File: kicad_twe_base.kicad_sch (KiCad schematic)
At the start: 9 parts, among them J1 Conn_01x14, J2 Conn_01x14, J3 Conn_01x07, SW1 SW_SPDT, SW2 SW_Push, SW3 SW_SPDT, U1 BHC-CR123A, U2 TWE-L-DP-W

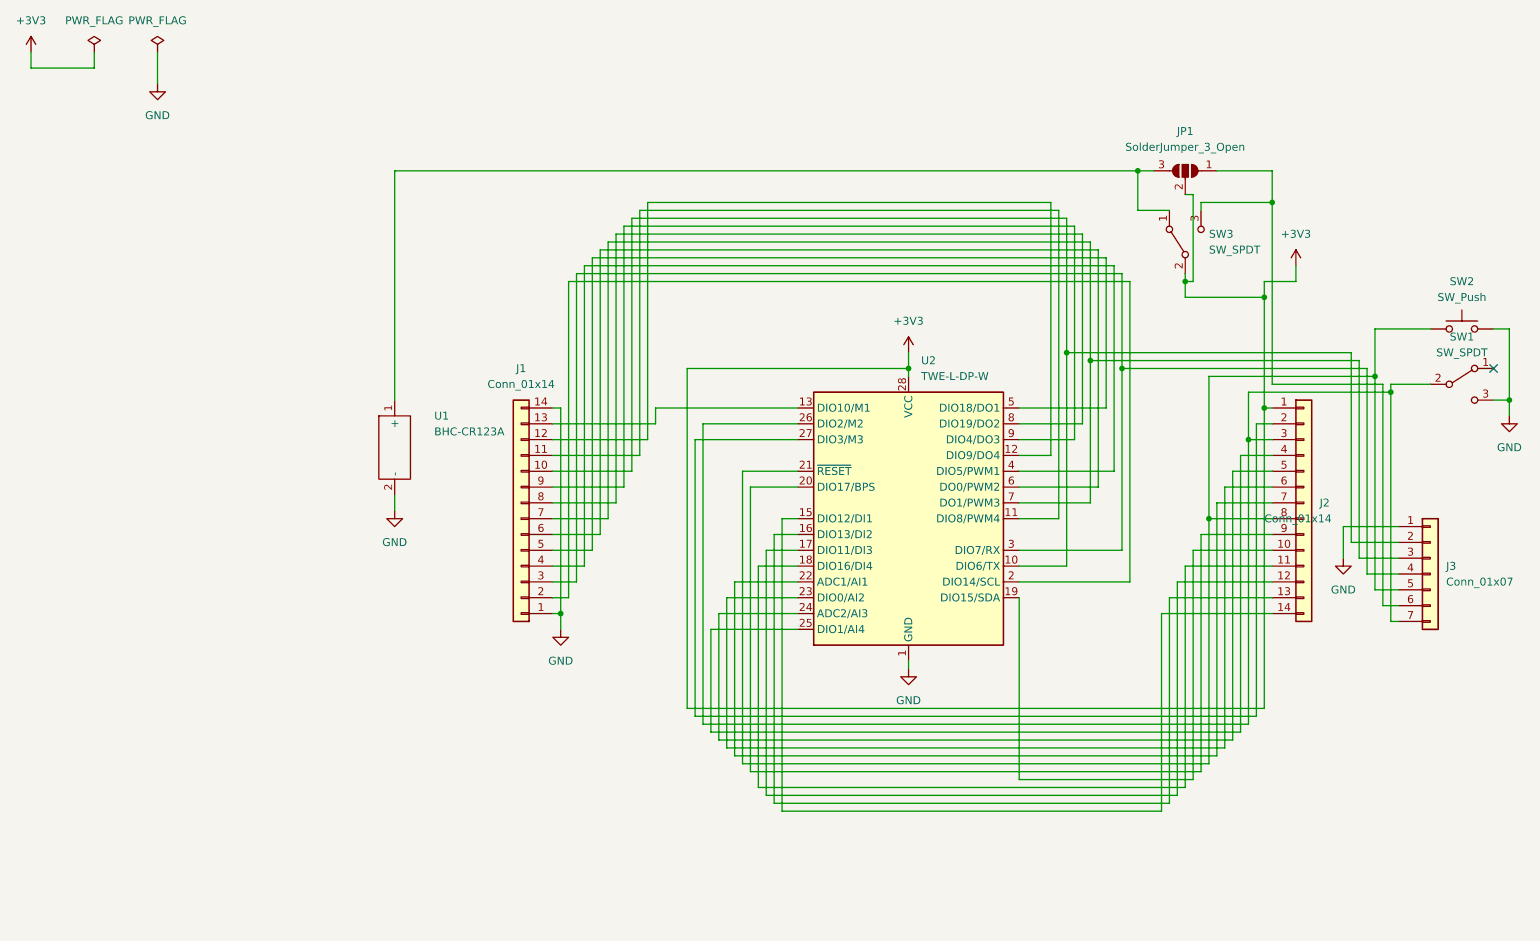
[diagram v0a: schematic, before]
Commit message: UART,I2Cのプルアップ抵抗を追加
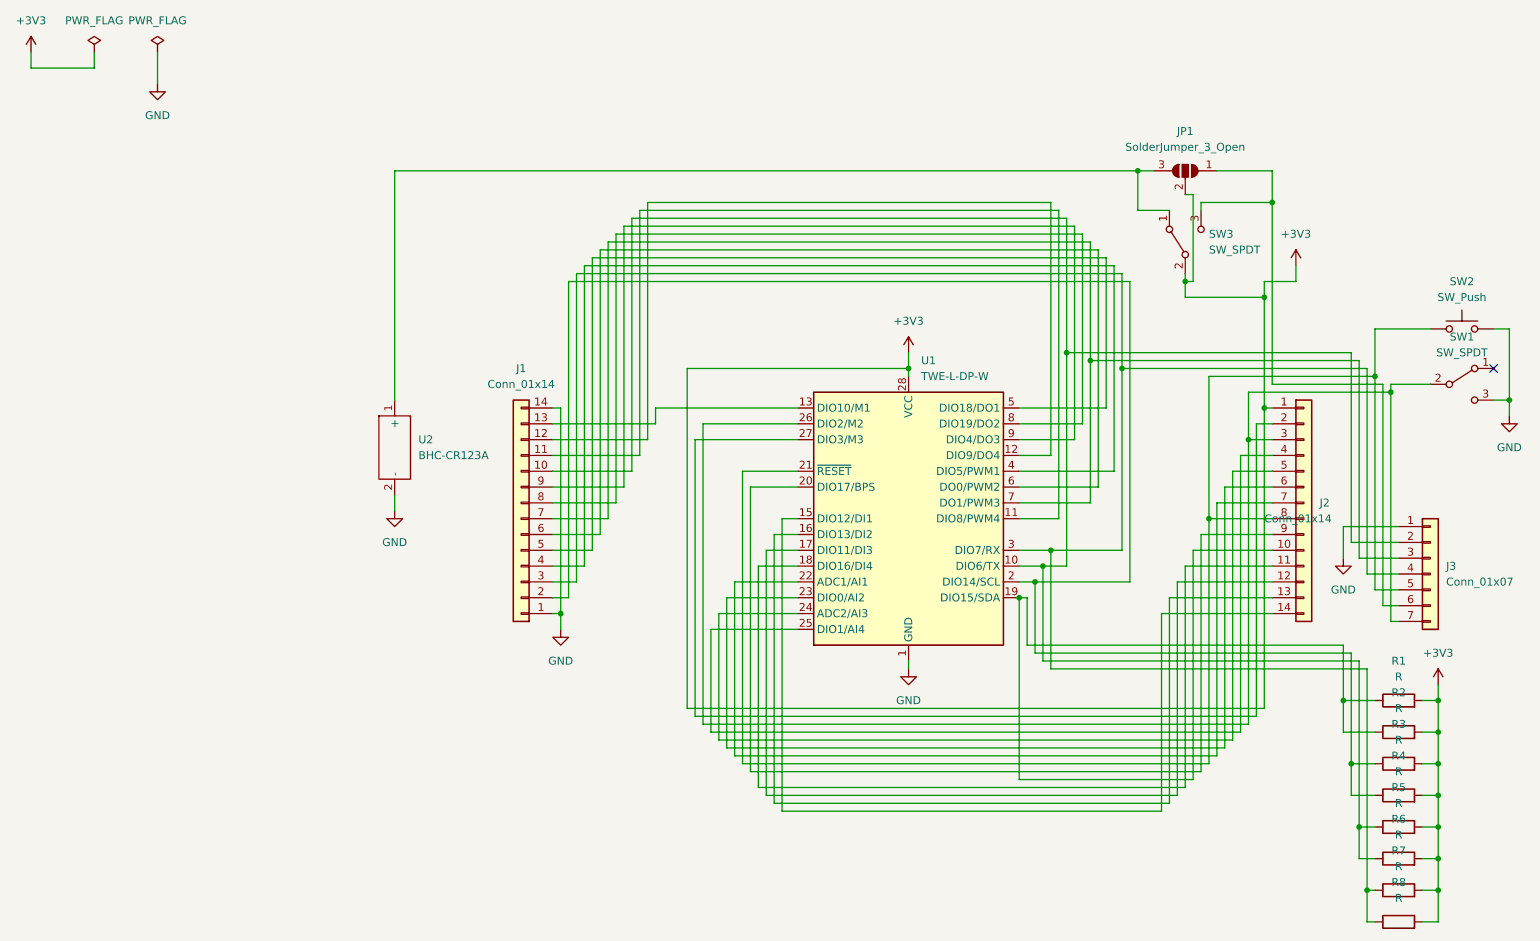
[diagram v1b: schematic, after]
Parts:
- added R1, R3, R5, R7: R, Resistor_THT:R_Axial_DIN0207_L6.3mm_D2.5mm_P10.16mm_Horizontal, symbol Device:R
- added R2, R4, R6, R8: R, Resistor_SMD:R_0603_1608Metric_Pad0.98x0.95mm_HandSolder, symbol Device:R
- renumbered U2 to U1, U1 to U2
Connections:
- net +3V3: now also R1.2, R2.2, R3.2, R4.2, R5.2, R6.2, R7.2, R8.2
- net at J1.10 (Pin_10), J3.2 (Pin_2), U1.10 (DIO6/TX): now also R5.1, R6.1
- net at J2.10 (Pin_10), U1.19 (DIO15/SDA): now also R1.1, R2.1
- net at J1.2 (Pin_2), U1.2 (DIO14/SCL): now also R3.1, R4.1
- net at J1.3 (Pin_3), J3.4 (Pin_4), U1.3 (DIO7/RX): now also R7.1, R8.1
